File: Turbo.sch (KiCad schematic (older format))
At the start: 15 parts, among them U12 74HCT27, U13 74HCT74, U14 74F86, U15 74F74, U16 74HCT04, U17 74HCT112, U18 74F157, U19 74F157

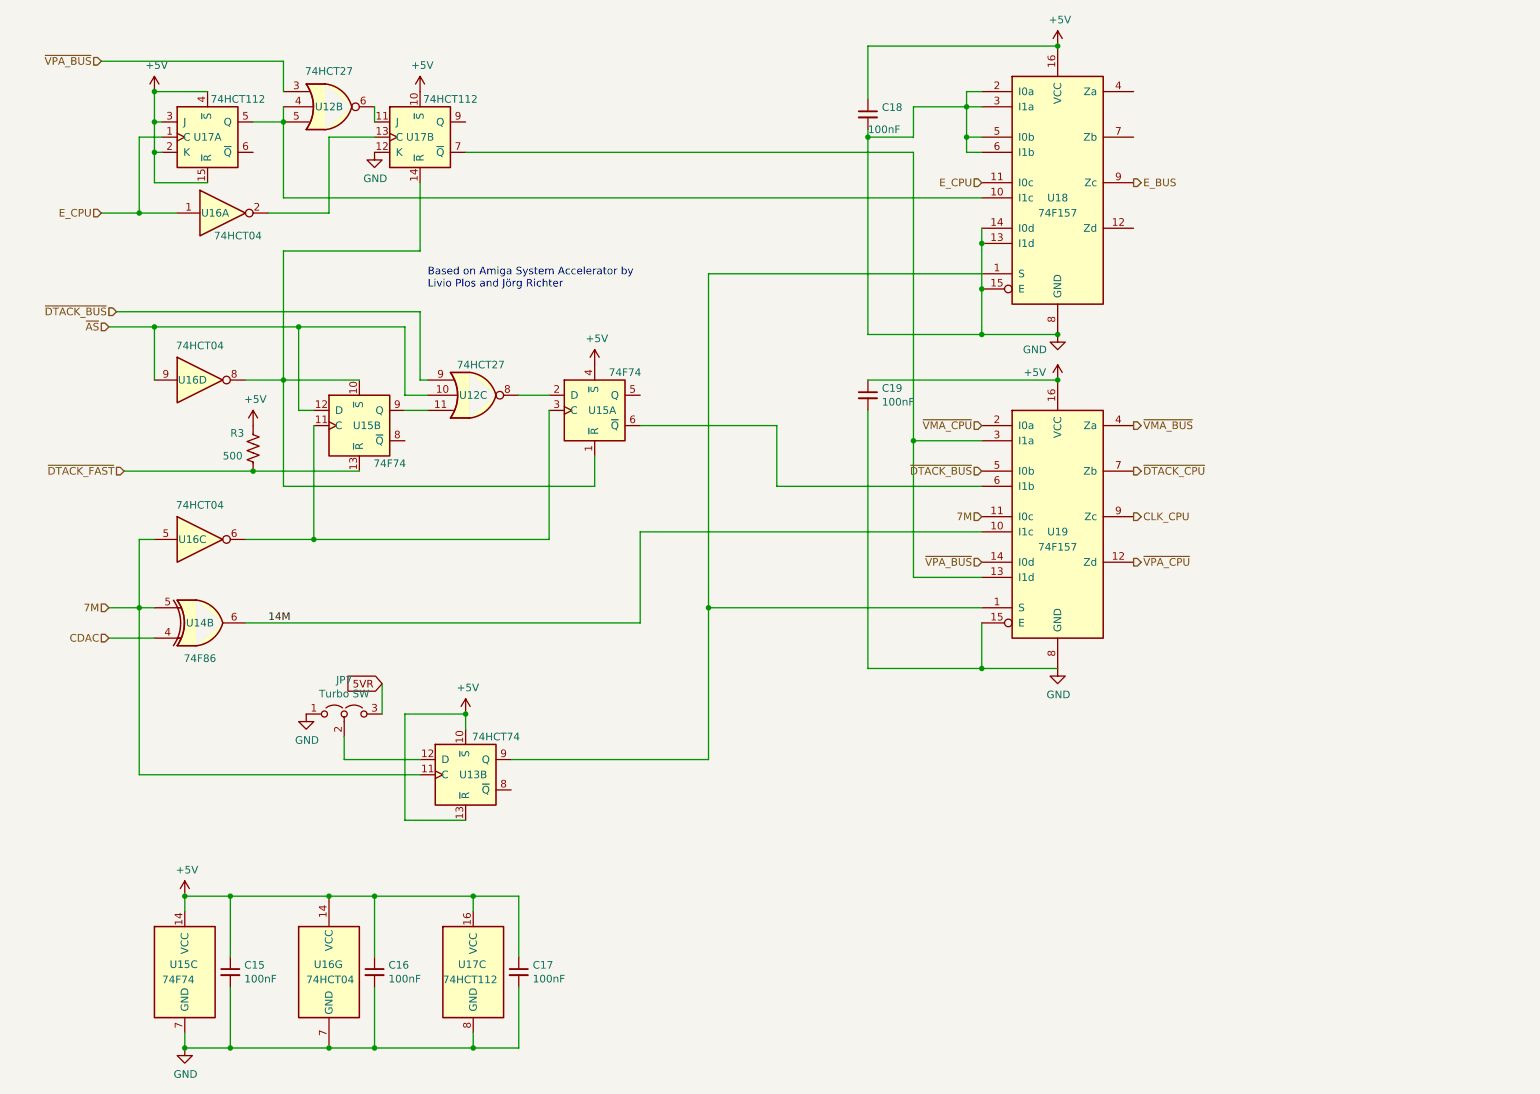
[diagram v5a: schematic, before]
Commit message: generate 7M from cdac schematics
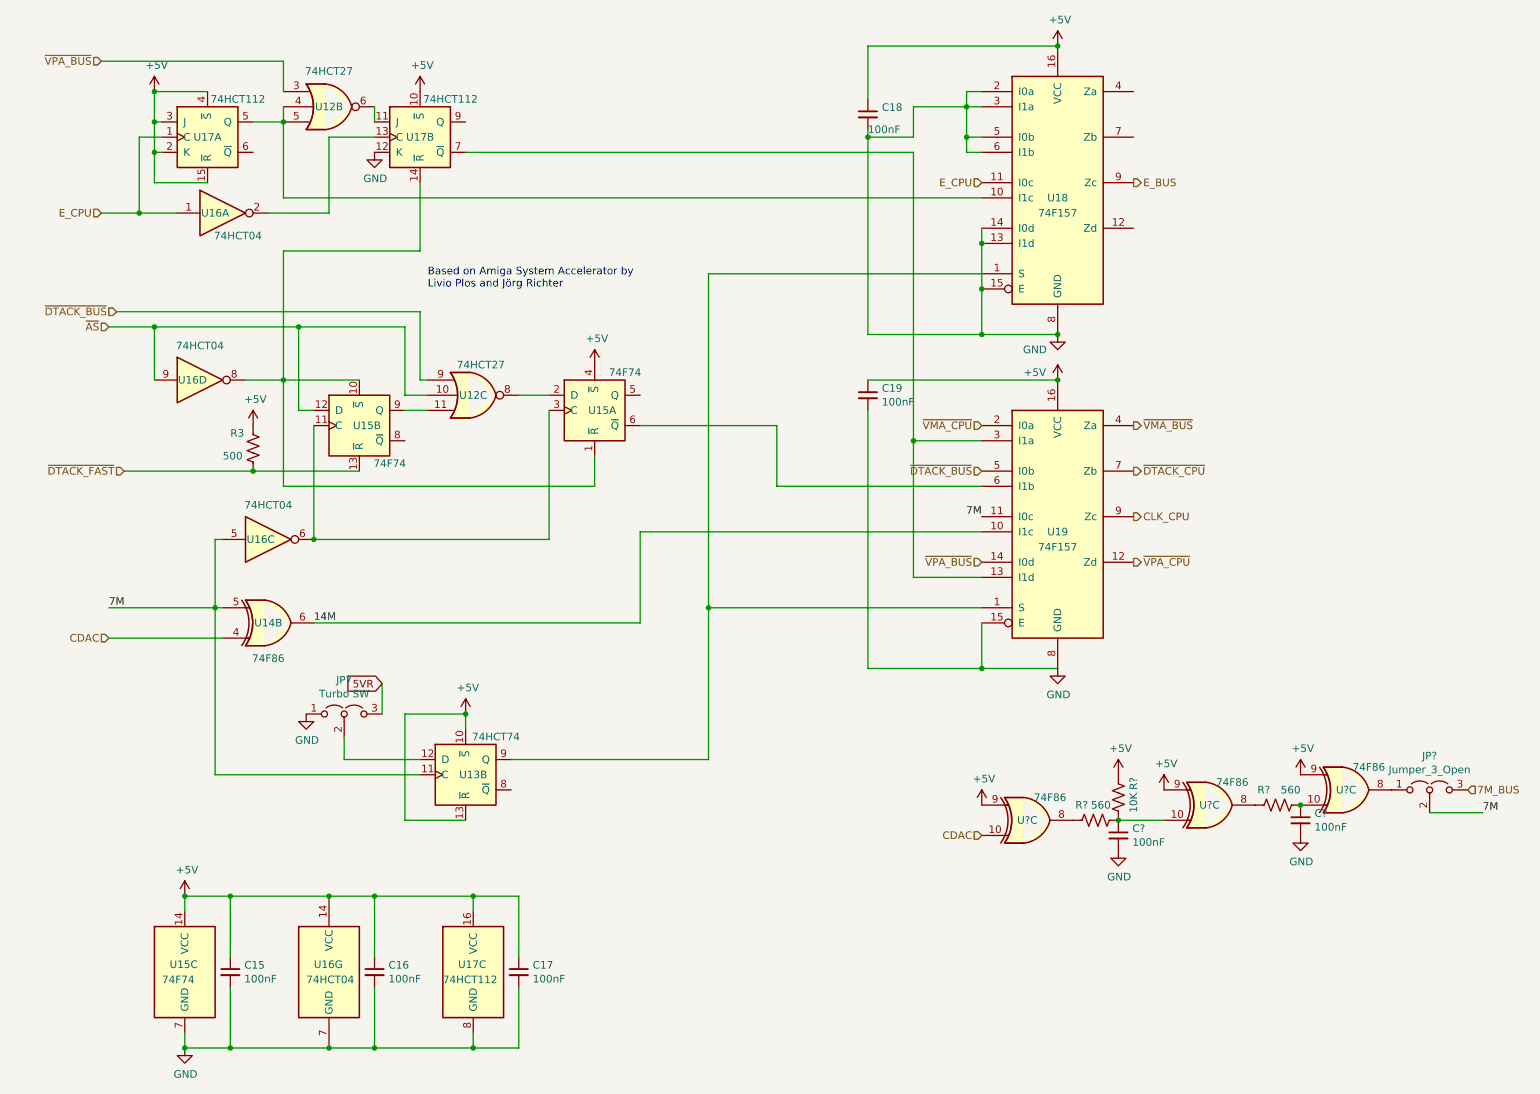
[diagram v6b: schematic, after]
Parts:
- added C? (x2): 100nF, Capacitor_THT:C_Disc_D7.0mm_W2.5mm_P5.00mm, symbol device:C_Small
- added JP?: Jumper_3_Open, symbol jumper:Jumper_3_Open
- added R? (x2): 560, Resistor_THT:R_Axial_DIN0411_L9.9mm_D3.6mm_P12.70mm_Horizontal, symbol device:R_US
- added R?: 10K, Resistor_THT:R_Axial_DIN0411_L9.9mm_D3.6mm_P12.70mm_Horizontal, symbol device:R_US
- added U? (x3): 74F86, Package_DIP:DIP-14_W7.62mm, symbol 74:74HC86
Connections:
- net +5V: now also R?.1, U?.9, U?.9, U?.9
- net 7M: now also JP?.2 (C)
- net CDAC: now also U?.10
- net GND: now also C?.2, C?.2
- new net: C?.1, R?.2, U?.10
- new net: JP?.1 (A), U?.8
- new net: R?.1, U?.8 (x2)
- new net: C?.1, R?.2, R?.2, U?.10
- new net 7M_BUS: JP?.3 (B)
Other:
- moved on the sheet: U14B, U16C

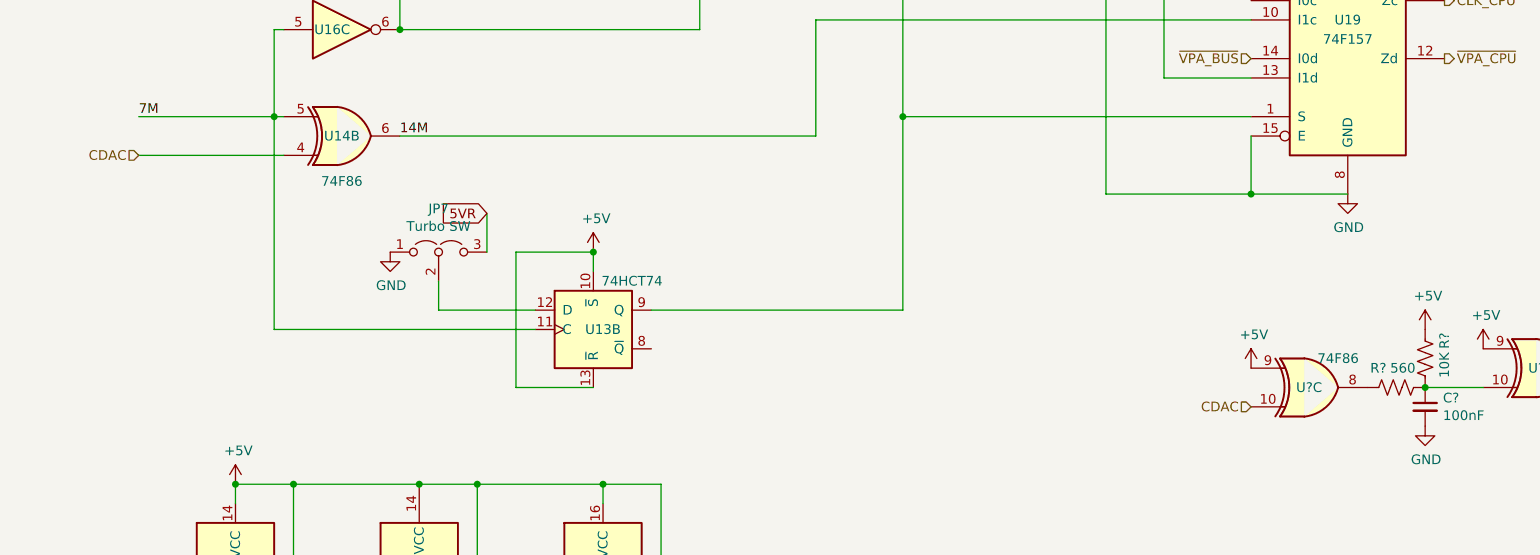
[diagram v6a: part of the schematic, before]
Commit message: use not cdac to invert 14M schematics
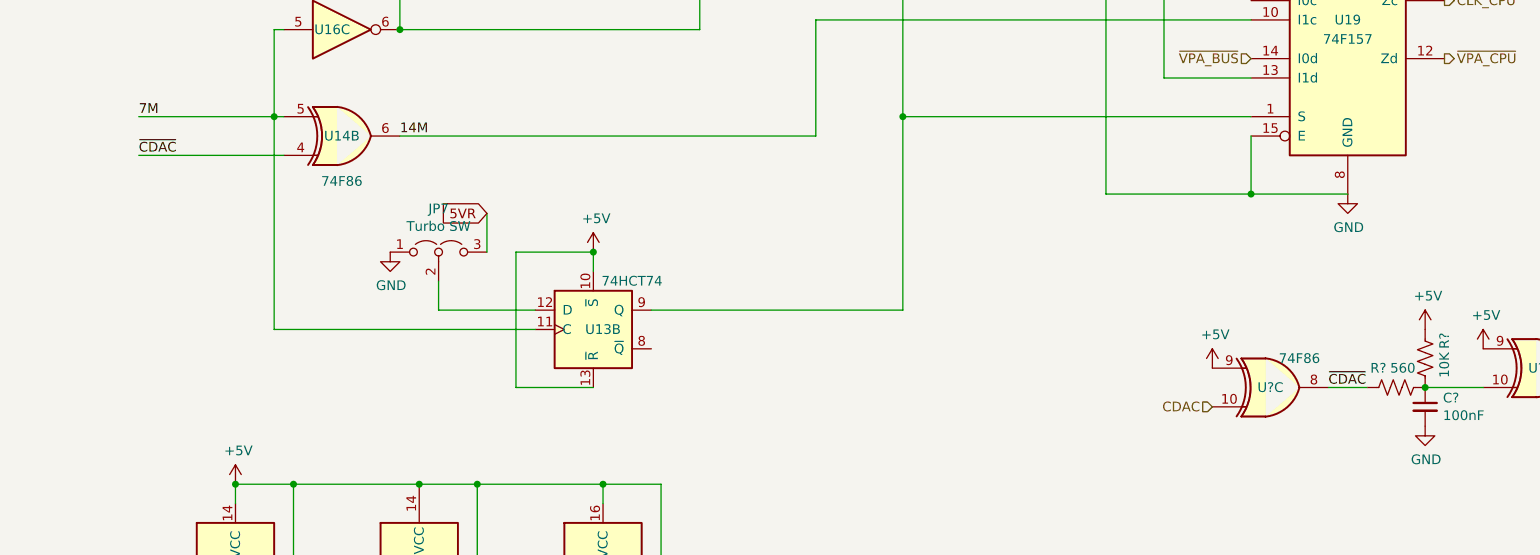
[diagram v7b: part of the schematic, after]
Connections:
- net CDAC: no longer U14.4
- net ~CDAC: now reaches R?.1, U?.8
- net ~CDAC: now also U14.4
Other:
- moved on the sheet: U?C
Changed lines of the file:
@@
 Comment4 ""
 $EndDescr
-Text HLabel 1050 4800 0    50   Input ~ 0
-CDAC
 Text HLabel 1100 2650 0    50   Input ~ 0
 ~DTACK_BUS
@@
 L 74:74HC86 U?
 U 3 1 612D5460
-P 7100 6000
+P 6900 6000
 AR Path="/606B7AE6/612D5460" Ref="U?"  Part="3"
 AR Path="/6068F728/612D5460" Ref="U?"  Part="3"
-F 0 "U?" H 7100 6000 50  0000 C CNN
-F 1 "74F86" H 7250 6150 50  0000 C CNN
-F 2 "Package_DIP:DIP-14_W7.62mm" H 7100 6000 50  0001 C CNN
-F 3 "http://www.ti.com/lit/gpn/sn74HC86" H 7100 6000 50  0001 C CNN
-	3    7100 6000
+F 0 "U?" H 6900 6000 50  0000 C CNN
+F 1 "74F86" H 7050 6150 50  0000 C CNN
+F 2 "Package_DIP:DIP-14_W7.62mm" H 6900 6000 50  0001 C CNN
+F 3 "http://www.ti.com/lit/gpn/sn74HC86" H 6900 6000 50  0001 C CNN
+	3    6900 6000
 	1    0    0    -1
 $EndComp
@@
 L OpenAmiga2000CoproAdapter-rescue:+5V-power #PWR?
 U 1 1 612DD220
-P 6800 5900
+P 6600 5900
 AR Path="/612DD220" Ref="#PWR?"  Part="1"
 AR Path="/6068F728/612DD220" Ref="#PWR?"  Part="1"
 AR Path="/606B7AE6/612DD220" Ref="#PWR?"  Part="1"
-F 0 "#PWR?" H 6800 5750 50  0001 C CNN
-F 1 "+5V" H 6815 6073 50  0000 C CNN
-F 2 "" H 6800 5900 50  0001 C CNN
-F 3 "" H 6800 5900 50  0001 C CNN
-	1    6800 5900
-	1    0    0    -1
-$EndComp
-Text HLabel 6800 6100 0    50   Input ~ 0
+F 0 "#PWR?" H 6600 5750 50  0001 C CNN
+F 1 "+5V" H 6615 6073 50  0000 C CNN
+F 2 "" H 6600 5900 50  0001 C CNN
+F 3 "" H 6600 5900 50  0001 C CNN
+	1    6600 5900
+	1    0    0    -1
+$EndComp
+Text HLabel 6600 6100 0    50   Input ~ 0
 CDAC
 $Comp
@@
 Wire Wire Line
 	9750 5950 10100 5950
+Wire Wire Line
+	7200 6000 7400 6000
+Text Label 7200 6000 0    50   ~ 0
+~CDAC
+Text Label 1050 4800 0    50   ~ 0
+~CDAC
 $EndSCHEMATC
